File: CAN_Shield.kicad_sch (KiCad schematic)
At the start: 17 parts, among them J1 GPIO, J2 KF128-2.54-4P, U1 MX128-5.08-09P-GN01-CU-Y-A, U2 MCP2515T-I/SO, U4 SN65HVD230DR, X1 X322516MLB4SI

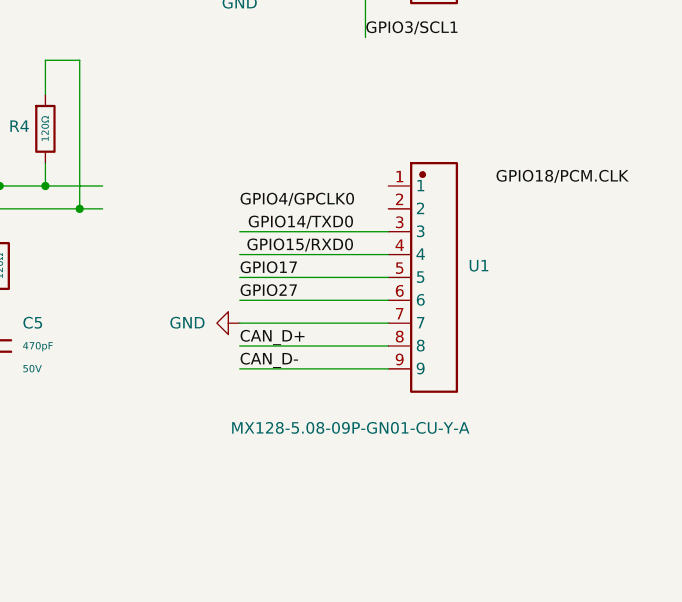
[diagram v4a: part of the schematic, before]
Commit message: rearrange pin order on 10 pin terminal block and copper fill
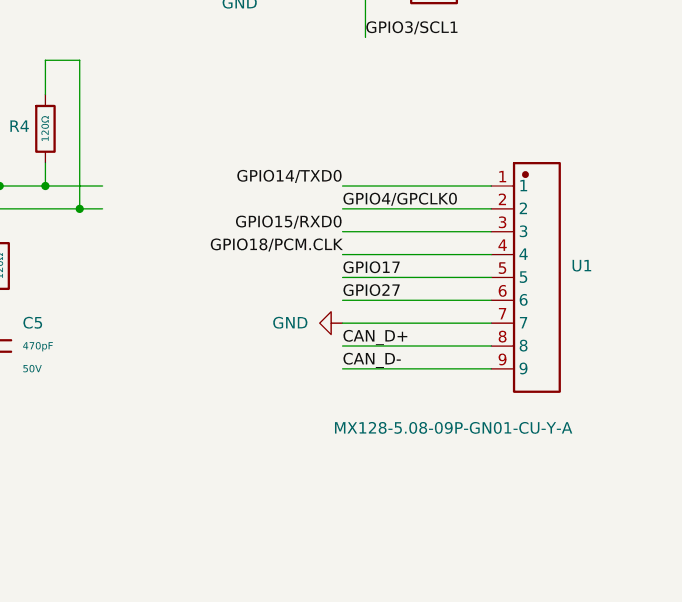
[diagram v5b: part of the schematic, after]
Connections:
- net GPIO14/TXD0: now also U1.1; no longer U1.3
- net GPIO15/RXD0: now also U1.3; no longer U1.4
- net GPIO18/PCM.CLK: now also U1.4
- net GPIO4/GPCLK0: now also U1.2
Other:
- moved on the sheet: U1
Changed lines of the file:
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@@
 	(wire
 		(pts
-			(xy 224.79 134.62) (xy 241.3 134.62)
+			(xy 236.22 134.62) (xy 252.73 134.62)
 		)
 		(stroke
@@
 	(wire
 		(pts
-			(xy 224.79 137.16) (xy 241.3 137.16)
+			(xy 236.22 137.16) (xy 252.73 137.16)
 		)
 		(stroke
@@
 	(wire
 		(pts
-			(xy 224.79 139.7) (xy 241.3 139.7)
+			(xy 236.22 139.7) (xy 252.73 139.7)
 		)
 		(stroke
@@
 	(wire
 		(pts
-			(xy 224.79 144.78) (xy 241.3 144.78)
+			(xy 236.22 144.78) (xy 252.73 144.78)
 		)
 		(stroke
@@
 	(wire
 		(pts
-			(xy 224.79 129.54) (xy 241.3 129.54)
+			(xy 236.22 129.54) (xy 252.73 129.54)
 		)
 		(stroke
@@
 	(wire
 		(pts
-			(xy 224.79 142.24) (xy 241.3 142.24)
+			(xy 236.22 142.24) (xy 252.73 142.24)
 		)
 		(stroke
@@
 	(wire
 		(pts
+			(xy 236.22 127) (xy 252.73 127)
+		)
+		(stroke
+			(width 0)
+			(type default)
+		)
+	)
+	(wire
+		(pts
 			(xy 22.86 72.39) (xy 52.07 72.39)
 		)
@@
 	(wire
 		(pts
+			(xy 236.22 124.46) (xy 252.73 124.46)
+		)
+		(stroke
+			(width 0)
+			(type default)
+		)
+	)
+	(wire
+		(pts
 			(xy 78.74 140.97) (xy 83.82 140.97)
 		)
@@
 	(wire
 		(pts
-			(xy 224.79 132.08) (xy 241.3 132.08)
+			(xy 236.22 132.08) (xy 252.73 132.08)
 		)
 		(stroke
@@
 	)
 	(label "GPIO4{slash}GPCLK0"
-		(at 224.79 127 0)
+		(at 236.22 127 0)
 		(effects
 			(font
@@
 	)
 	(label "GPIO15{slash}RXD0"
-		(at 237.49 132.08 180)
+		(at 236.22 129.54 180)
 		(effects
 			(font
@@
 	)
 	(label "GPIO27"
-		(at 224.79 137.16 0)
+		(at 236.22 137.16 0)
 		(effects
 			(font
@@
 	)
 	(label "GPIO14{slash}TXD0"
-		(at 237.49 129.54 180)
+		(at 236.22 124.46 180)
 		(effects
 			(font
@@
 	)
 	(label "GPIO17"
-		(at 224.79 134.62 0)
+		(at 236.22 134.62 0)
 		(effects
 			(font
@@
 	)
 	(label "GPIO18{slash}PCM.CLK"
-		(at 267.97 124.46 180)
+		(at 236.22 132.08 180)
 		(effects
 			(font
@@
 	)
 	(label "CAN_D+"
-		(at 224.79 142.24 0)
+		(at 236.22 142.24 0)
 		(effects
 			(font
@@
 	)
 	(label "CAN_D-"
-		(at 224.79 144.78 0)
+		(at 236.22 144.78 0)
 		(effects
 			(font
@@
 		(lib_name "GND_4")
 		(lib_id "power:GND")
-		(at 224.79 139.7 270)
+		(at 236.22 139.7 270)
 		(unit 1)
 		(exclude_from_sim no)
@@
 		(fields_autoplaced yes)
 		(property "Reference" "#PWR6"
-			(at 218.44 139.7 0)
+			(at 229.87 139.7 0)
 			(effects
 				(font
@@
 		)
 		(property "Value" "GND"
-			(at 220.98 139.6999 90)
+			(at 232.41 139.6999 90)
 			(effects
 				(font
@@
 		)
 		(property "Footprint" ""
-			(at 224.79 139.7 0)
+			(at 236.22 139.7 0)
 			(effects
 				(font
@@
 		)
 		(property "Datasheet" ""
-			(at 224.79 139.7 0)
+			(at 236.22 139.7 0)
 			(effects
 				(font
@@
 		)
 		(property "Description" "Power symbol creates a global label with name \"GND\" , ground"
-			(at 224.79 139.7 0)
+			(at 236.22 139.7 0)
 			(effects
 				(font
@@
 	(symbol
 		(lib_id "ImportSymbol:MX128-5.08-09P-GN01-CU-Y-A")
-		(at 246.38 134.62 0)
+		(at 257.81 134.62 0)
 		(unit 1)
 		(exclude_from_sim no)
@@
 		(dnp no)
 		(property "Reference" "U1"
-			(at 250.19 133.3499 0)
+			(at 261.62 133.3499 0)
 			(effects
 				(font
@@
 		)
 		(property "Value" "MX128-5.08-09P-GN01-CU-Y-A"
-			(at 223.774 151.384 0)
+			(at 235.204 151.384 0)
 			(effects
 				(font
@@
 		)
 		(property "Footprint" "ImportFP:CONN-TH_9P-P5.08_MX128-5.08-09P-GN01-CU-Y-A"
-			(at 246.38 134.62 0)
+			(at 257.81 134.62 0)
 			(effects
 				(font
@@
 		)
 		(property "Datasheet" ""
-			(at 246.38 134.62 0)
+			(at 257.81 134.62 0)
 			(effects
 				(font
@@
 		)
 		(property "Description" ""
-			(at 246.38 134.62 0)
+			(at 257.81 134.62 0)
 			(effects
 				(font
@@
 		)
 		(property "Manufacturer Part" "MX128-5.08-09P-GN01-Cu-Y-A"
-			(at 246.38 134.62 0)
+			(at 257.81 134.62 0)
 			(effects
 				(font
@@
 		)
 		(property "Manufacturer" "MAX(迈旭)"
-			(at 246.38 134.62 0)
+			(at 257.81 134.62 0)
 			(effects
 				(font
@@
 		)
 		(property "Supplier Part" "C5290382"
-			(at 246.38 134.62 0)
+			(at 257.81 134.62 0)
 			(effects
 				(font
@@
 		)
 		(property "Supplier" "LCSC"
-			(at 246.38 134.62 0)
+			(at 257.81 134.62 0)
 			(effects
 				(font

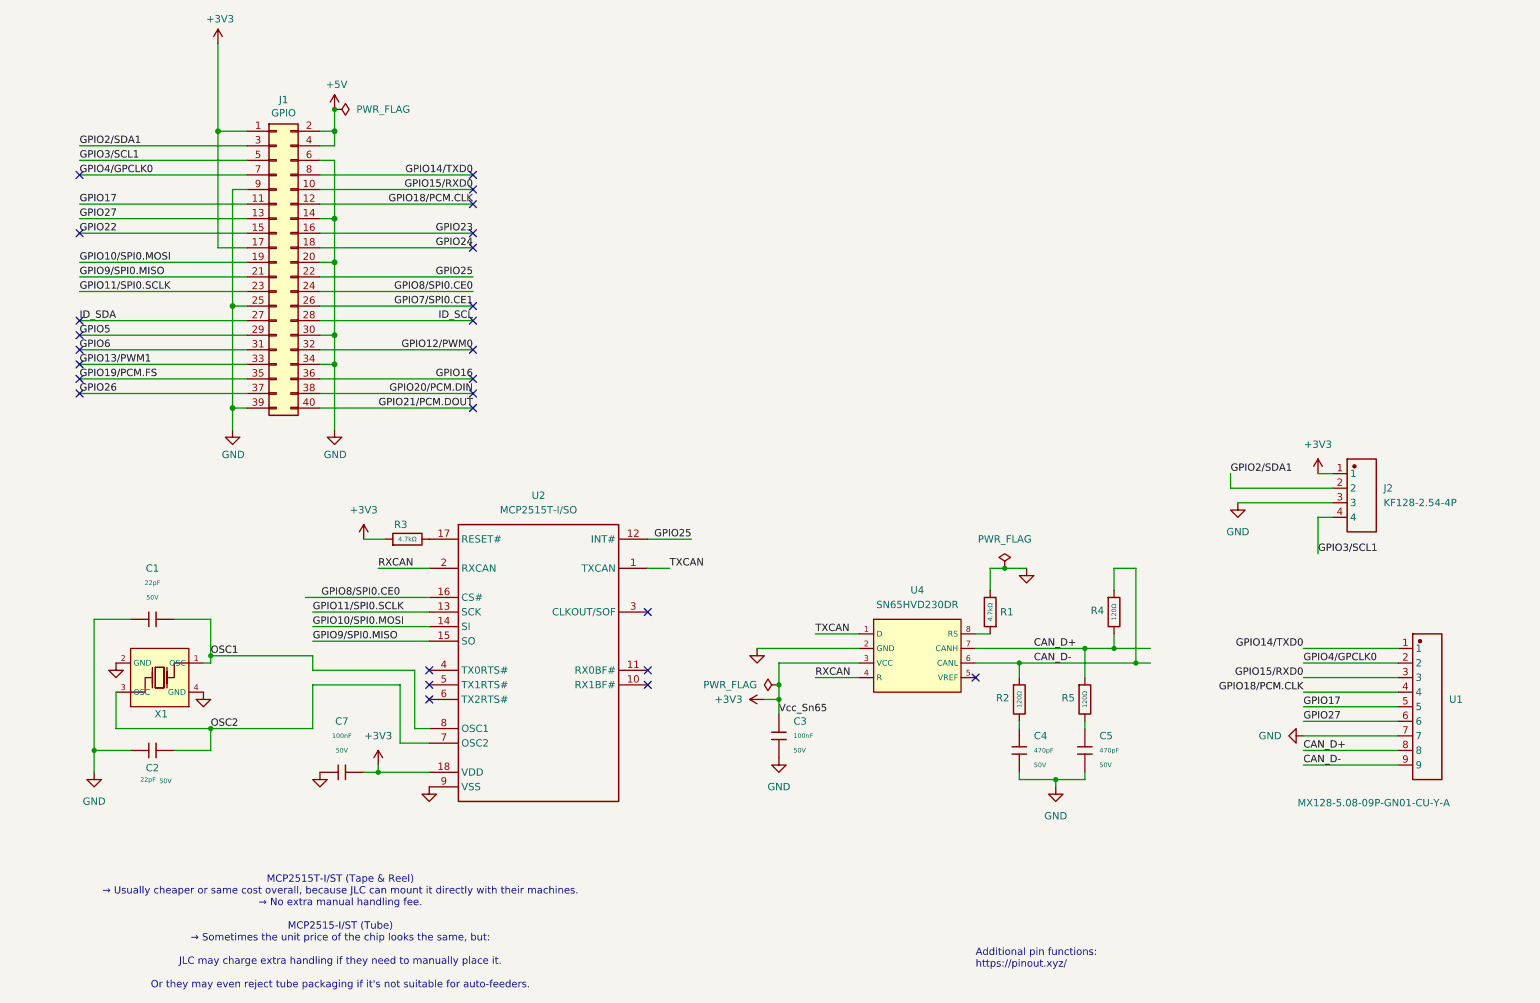
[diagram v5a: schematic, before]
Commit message: finished schematics and layout for 3 terminal block except CAN
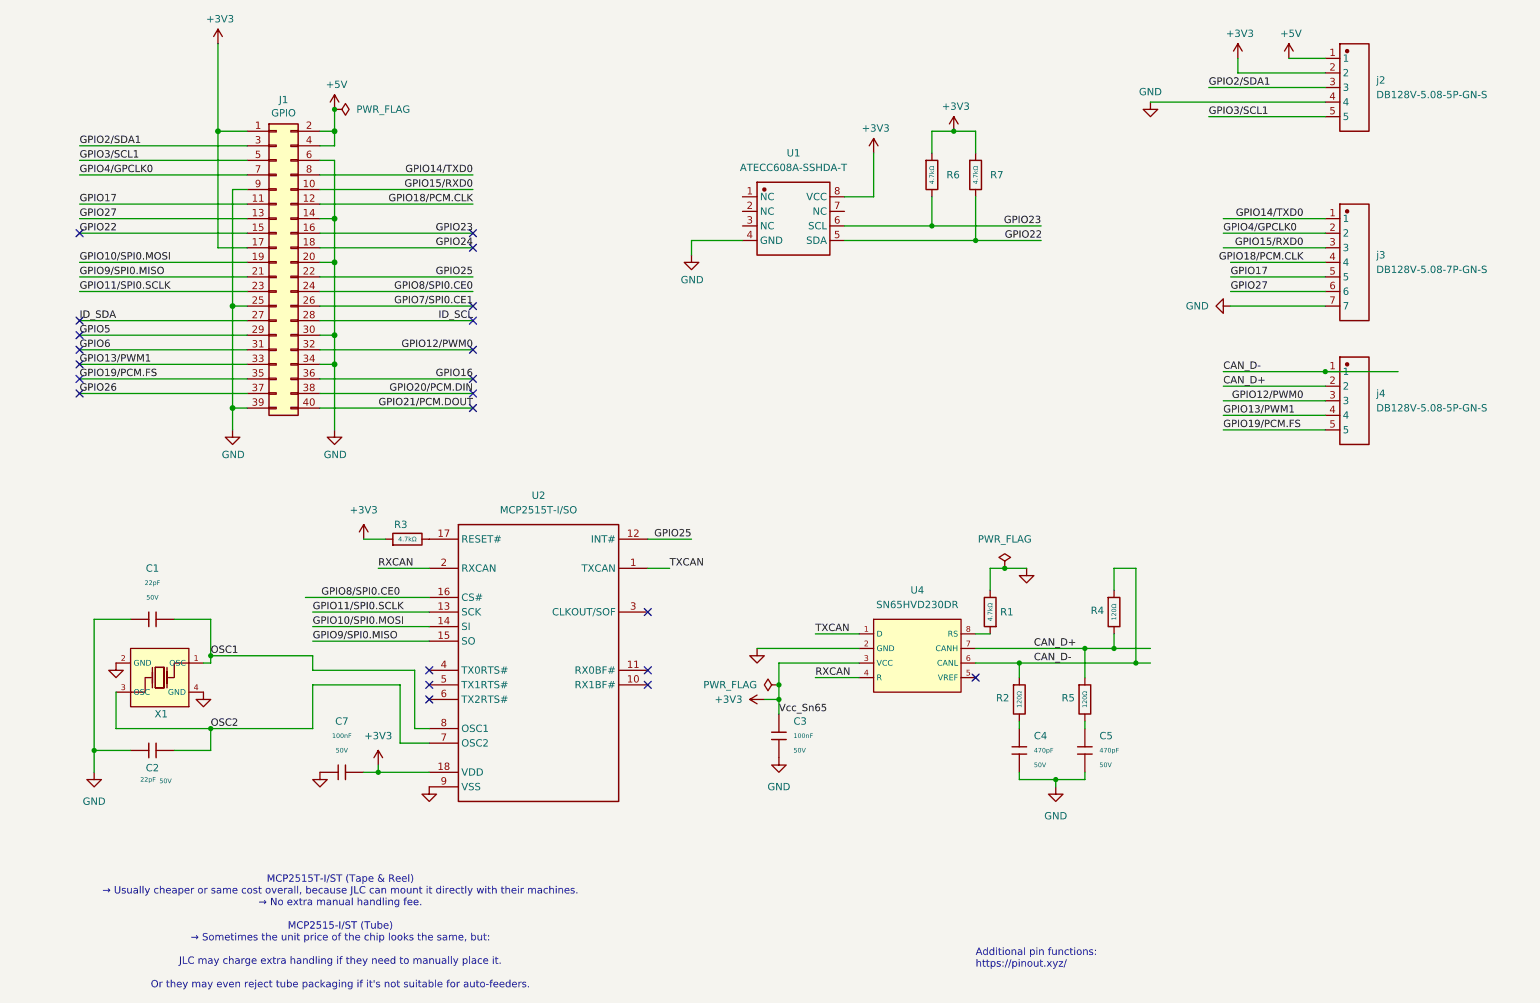
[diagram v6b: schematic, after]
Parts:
- removed J2: KF128-2.54-4P, ImportFP:CONN-TH_4P-P2.54_KF128-2.54-4P, symbol ImportSymbol:KF128-2.54-4P
- removed U1: MX128-5.08-09P-GN01-CU-Y-A, ImportFP:CONN-TH_9P-P5.08_MX128-5.08-09P-GN01-CU-Y-A, symbol ImportSymbol:MX128-5.08-09P-GN01-CU-Y-A
- added R6, R7: 4.7kΩ, PCM_JLCPCB:R_0402, symbol PCM_JLCPCB-Resistors:0402,4.7kΩ
- added U1: ATECC608A-SSHDA-T, ImportFP:MICROCHIP ATECC608A-SSHDA-T, symbol ImportSymbol:ATECC608A-SSHDA-T_C616024
- added j2, j4: DB128V-5.08-5P-GN-S, ImportFP:CONN-TH_5P-P5.08_DIBO_DB128V-5.08-5P-GN-S, symbol ImportSymbol:DB128V-5.08-5P-GN-S
- added j3: DB128V-5.08-7P-GN-S, ImportFP:CONN-TH_7P-P5.08_DIBO_DB128V-5.08-7P-GN-S, symbol ImportSymbol:DB128V-5.08-7P-GN-S
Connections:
- net +3V3: now also R6.1, R7.1, U1.8 (VCC), j2.2
- net +5V: now also j2.1
- net CAN_D+: now also j4.2
- net CAN_D-: now also j4.1
- net GND: now also U1.4 (GND), j2.4, j3.7
- net GPIO12/PWM0: now also j4.3
- net GPIO13/PWM1: now also j4.4
- net GPIO14/TXD0: now also j3.1
- net GPIO15/RXD0: now also j3.3
- net GPIO17: now also j3.5
- net GPIO18/PCM.CLK: now also j3.4
- net GPIO19/PCM.FS: now also j4.5
- net GPIO22: now also R7.2, U1.5 (SDA)
- net GPIO23: now also R6.2, U1.6 (SCL)
- net GPIO27: now also j3.6
- net GPIO2/SDA1: now also j2.3
- net GPIO3/SCL1: now also j2.5
- net GPIO4/GPCLK0: now also j3.2
- no-connect marks 26 -> 22

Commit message: increase terminal block and 40 pin header spacing for easy soldering, also use DB-7P instead of 8 pin, add ESD diode for CAN
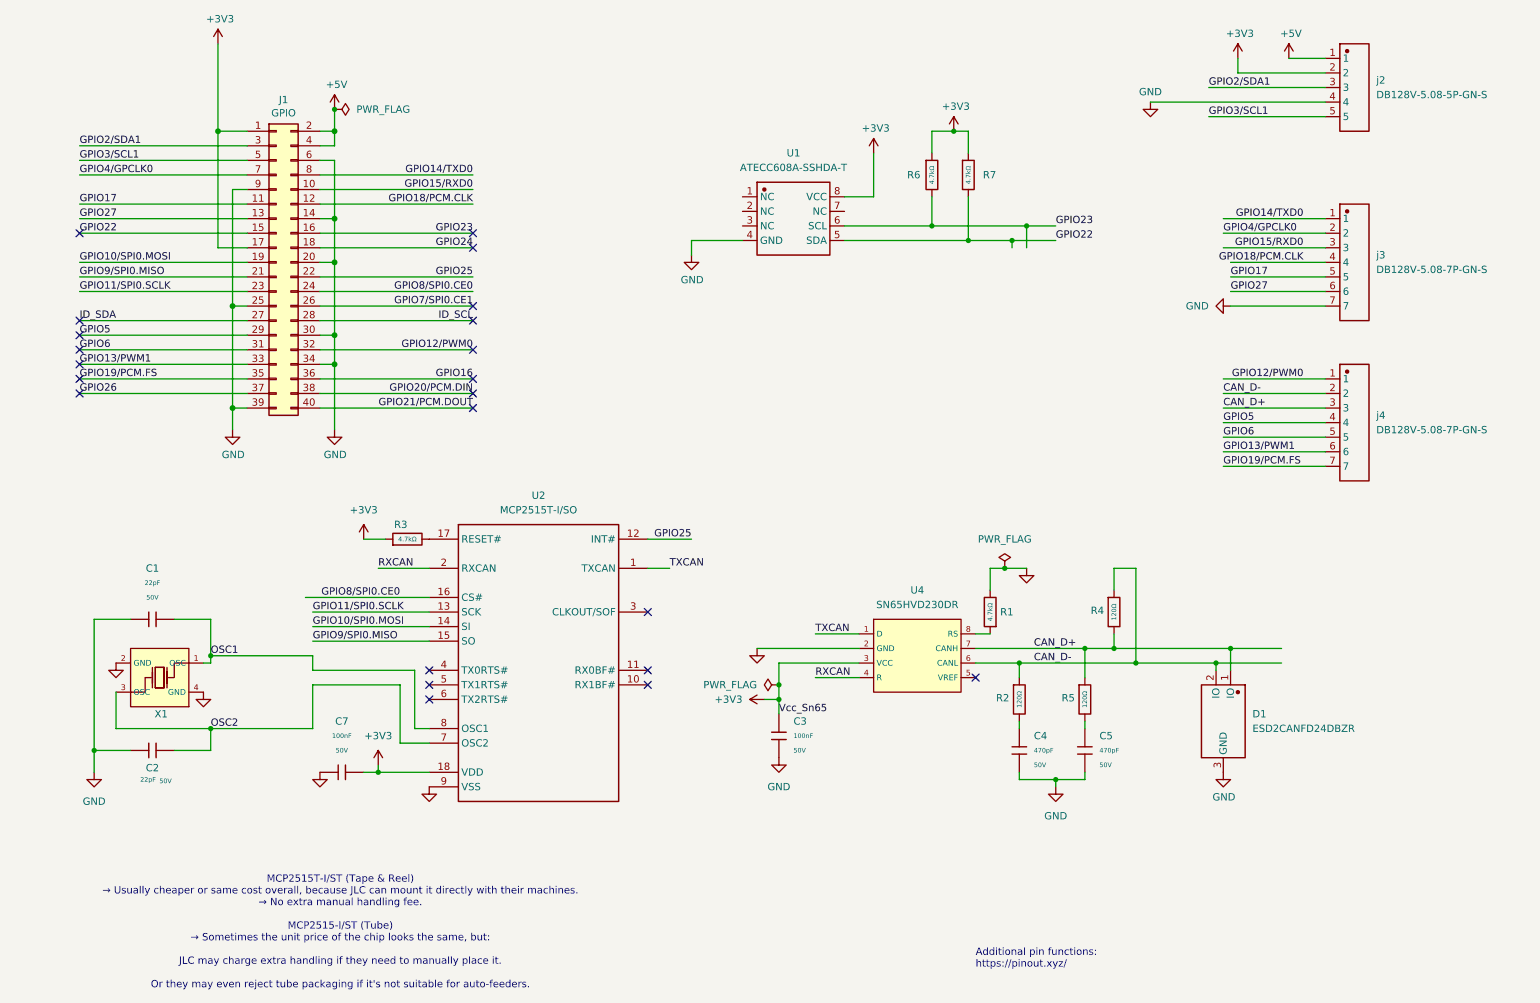
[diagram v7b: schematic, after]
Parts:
- removed j4: DB128V-5.08-5P-GN-S, ImportFP:CONN-TH_5P-P5.08_DIBO_DB128V-5.08-5P-GN-S, symbol ImportSymbol:DB128V-5.08-5P-GN-S
- added D1: ESD2CANFD24DBZR, ImportFP:TI ESD2CANFD24DBZR, symbol ImportSymbol:ESD2CANFD24DBZR
- added j4: DB128V-5.08-7P-GN-S, ImportFP:CONN-TH_7P-P5.08_DIBO_DB128V-5.08-7P-GN-S, symbol ImportSymbol:DB128V-5.08-7P-GN-S
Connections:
- net CAN_D+: now also D1.1 (IO), j4.3
- net CAN_D-: now also D1.2 (IO), j4.2
- net GND: now also D1.3 (GND)
- net GPIO12/PWM0: now also j4.1
- net GPIO13/PWM1: now also j4.6
- net GPIO19/PCM.FS: now also j4.7
- net GPIO5: now also j4.4
- net GPIO6: now also j4.5
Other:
- moved on the sheet: R7

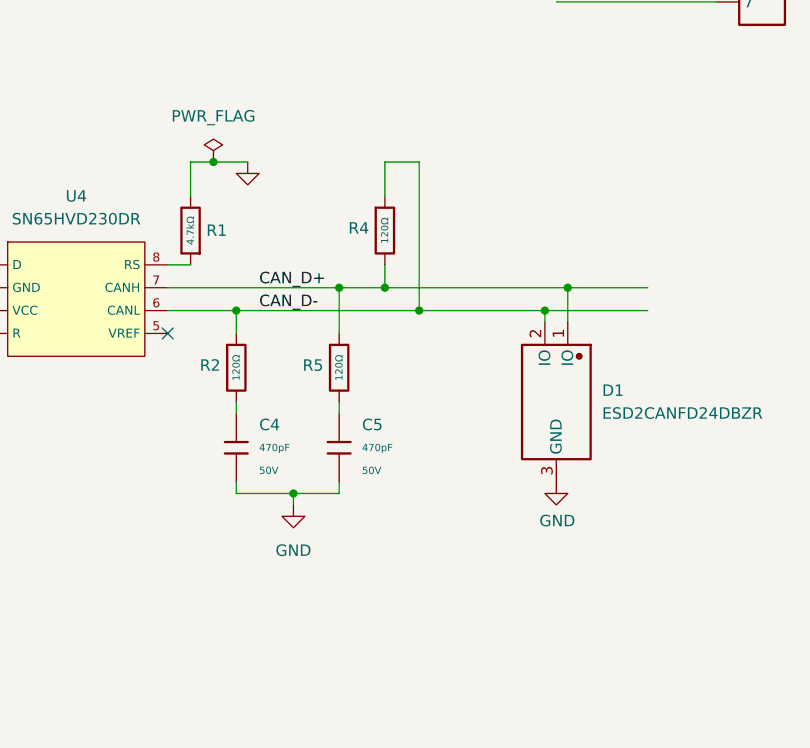
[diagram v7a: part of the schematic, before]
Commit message: finished can split termination and TVS diode layout
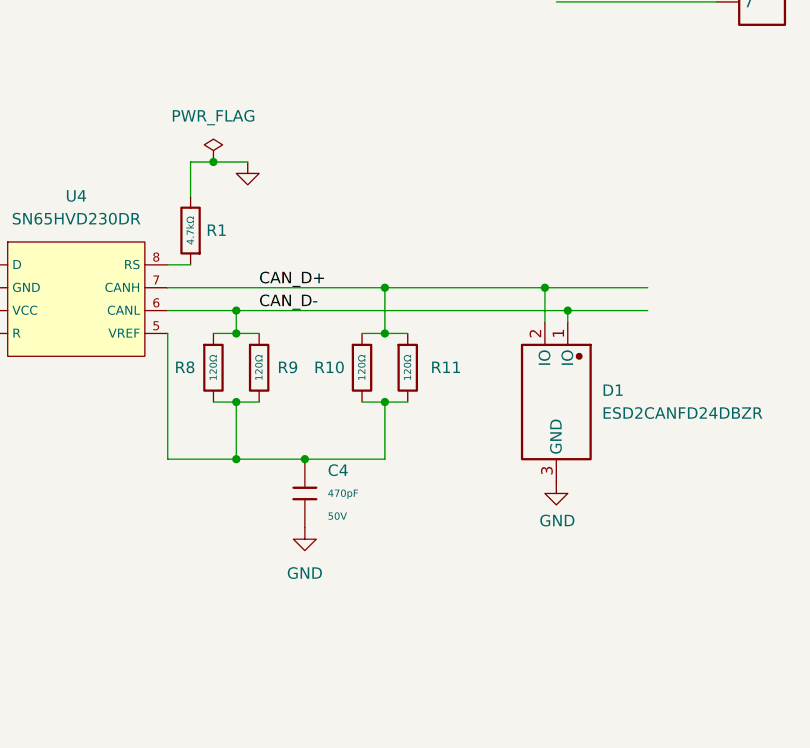
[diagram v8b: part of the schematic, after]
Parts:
- removed C5: 470pF, PCM_JLCPCB:C_0402, symbol PCM_JLCPCB-Capacitors:0402,470pF
- removed R2, R4, R5: 120Ω, PCM_JLCPCB:R_0603, symbol PCM_JLCPCB-Resistors:0603,120Ω
- added R10, R11, R8, R9: 120Ω, PCM_JLCPCB:R_0402, symbol PCM_JLCPCB-Resistors:0402,120Ω
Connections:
- net CAN_D+: now also D1.2 (IO), R10.1, R11.1; no longer D1.1 (IO)
- net CAN_D-: now also D1.1 (IO), R8.1, R9.1; no longer D1.2 (IO)
- net at C4.1: now also U4.5 (VREF), R10.2, R11.2, R8.2, R9.2
- no-connect marks 22 -> 21
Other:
- moved on the sheet: C4
